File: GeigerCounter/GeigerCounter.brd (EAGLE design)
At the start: 100 x 80 mm, 5 parts, among them IC1 OPAMP-DUALU

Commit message: preliminary schematic work
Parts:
- added C2, C3, C4, C5, C6: (no value), SparkFun-Passives:CAP-PTH-SMALL2
- added H1, H2, H3, H4: MOUNT-HOLE3.0, holes:3,0
- added IC2: OPAMP-DUALU, SparkFun-AnalogIC:SO08
- added R10, R11, R12, R13, R14, R15, R16, R18, R19, R2, R20, R22, R3, R4, R5, R6, R7, R8, R9: (no value), SparkFun-Passives:AXIAL-0.3
- moved C1 68.7 mm to (-53.5, -47.4)
- moved R1 64.9 mm to (-44.7, -43.7)
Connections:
- removed net V+: IC1.8
- removed net V-: IC1.4
- new net N$1: C3.2, R3.P$1
- new net N$10: C4.2, IC2.1, R12.P$2, R14.P$2, R15.P$1
- new net N$11: C4.1, IC2.2, R12.P$1, R14.P$1
- new net N$12: C5.1, R15.P$2
- new net N$13: C5.2, R13.P$1
- new net N$14: C6.1, IC2.6, R18.P$1, R19.P$1, R8.P$2
- new net N$15: C6.2, IC2.7, R18.P$2, R19.P$2, R20.P$1
- new net N$2: D1.A, R9.P$1
- new net N$3: C2.2, IC1.1, R10.P$2, R11.P$1, R2.P$2
- new net N$4: IC2.5, R13.P$2, R16.P$2
- new net N$5: D1.C, R22.P$1
- new net N$6: C2.1, IC1.2, R10.P$1, R2.P$1
- new net N$7: C3.1, R11.P$2
- new net N$8: C1.1, IC1.6, R3.P$2, R5.P$1, R6.P$1
- new net N$9: C1.2, IC1.7, R5.P$2, R6.P$2, R7.P$1
- new net VCC_1.25: IC1.3, IC1.5, R1.P$2, R4.P$1
- net GND: now also IC1.4, IC2.3, IC2.4, R1.P$1, R16.P$1, R8.P$1
- net VCC: now also IC1.8, IC2.8, R4.P$2

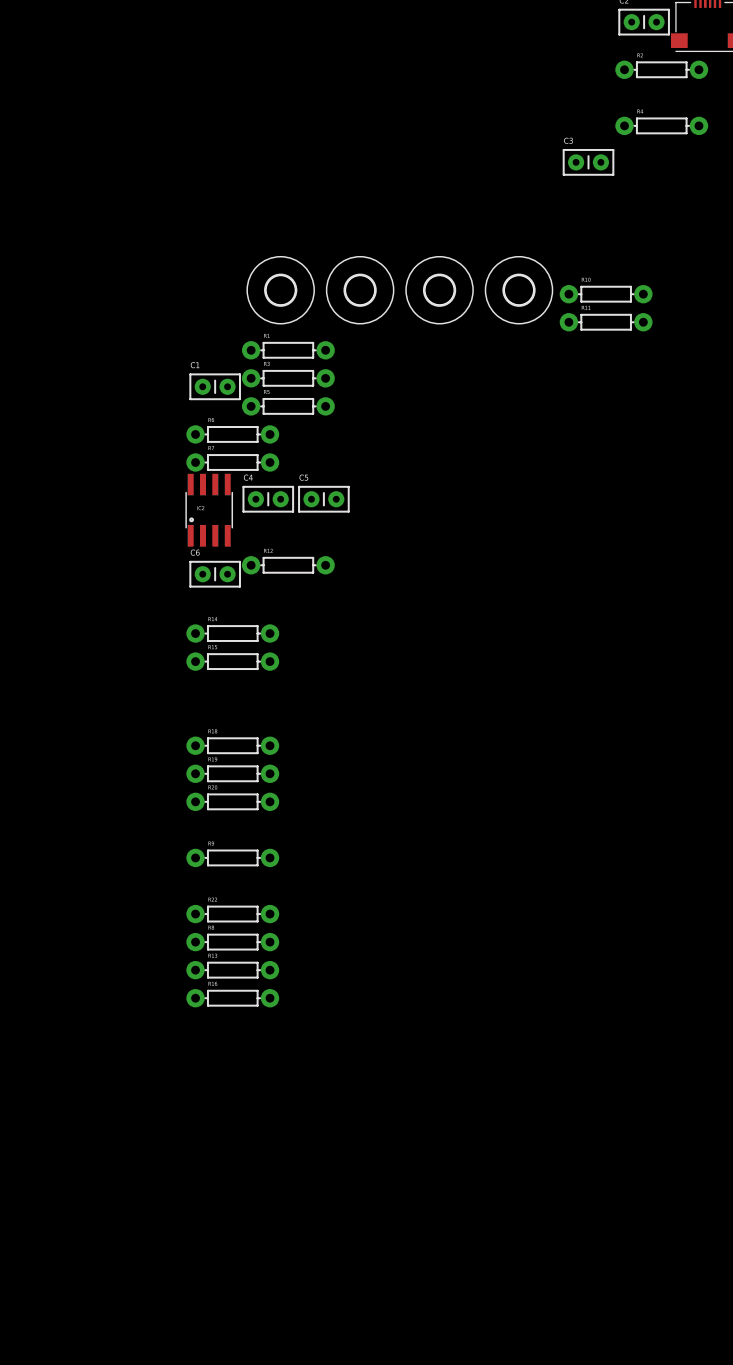
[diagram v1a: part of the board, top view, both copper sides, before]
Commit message: all components placed in schematic
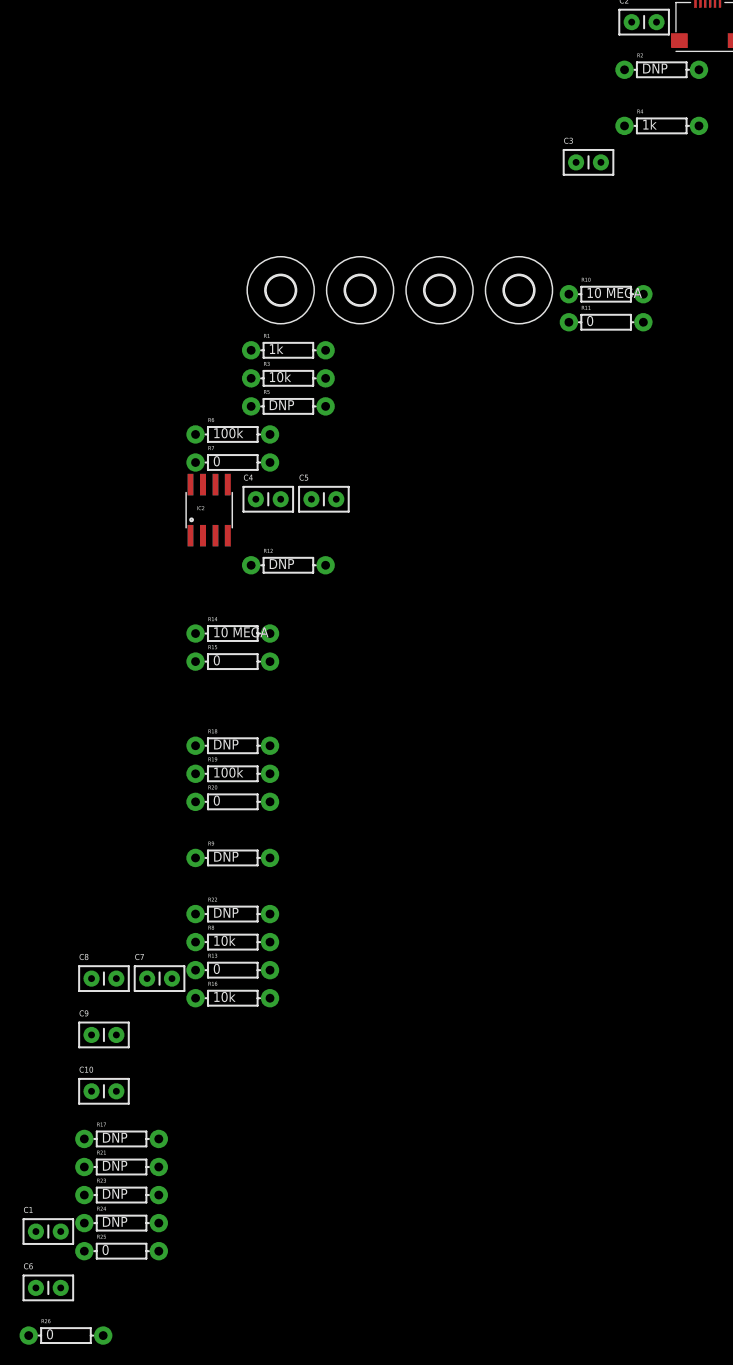
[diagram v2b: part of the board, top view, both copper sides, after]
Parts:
- added C10, C8: 0.1uF, SparkFun-Passives:CAP-PTH-SMALL2
- added C7, C9: 2.2uF, SparkFun-Passives:CAP-PTH-SMALL2
- added R17, R21, R23, R24: DNP, SparkFun-Passives:AXIAL-0.3
- added R25, R26: 0, SparkFun-Passives:AXIAL-0.3
- C1, C6, R12, R18, R2, R22, R5, R9: value (none) -> DNP
- C2, C4: value (none) -> 2pF
- C3, C5: value (none) -> 100pF
- R1, R4: value (none) -> 1k
- R10, R14: value (none) -> 10 MEGA
- R11, R13, R15, R20, R7: value (none) -> 0
- R16, R3, R8: value (none) -> 10k
- R19, R6: value (none) -> 100k
- moved C1 88.1 mm to (-70.6, -133.9)
- moved C6 75.0 mm to (-70.6, -139.6)
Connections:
- new net N$16: R26.P$1, R7.P$2
- new net N$17: C1.1, R24.P$1, R25.P$2
- new net N$20: C6.1, R23.P$1, R26.P$2
- new net N$21: R20.P$2, R25.P$1
- net GND: now also C1.2, C10.1, C6.2, C7.1, C8.1, C9.1, R9.P$2
- net N$11: now also R21.P$2
- net N$14: no longer C6.1
- net N$15: no longer C6.2
- net N$2: now also R17.P$1
- net N$5: now also R21.P$1
- net N$6: now also R17.P$2
- net N$8: no longer C1.1
- net N$9: no longer C1.2
- net P3.4: now also R24.P$2
- net P3.5: now also R23.P$2
- net VCC: now also C10.2, C7.2, C8.2, C9.2
- net VCC_1.25: now also R22.P$2

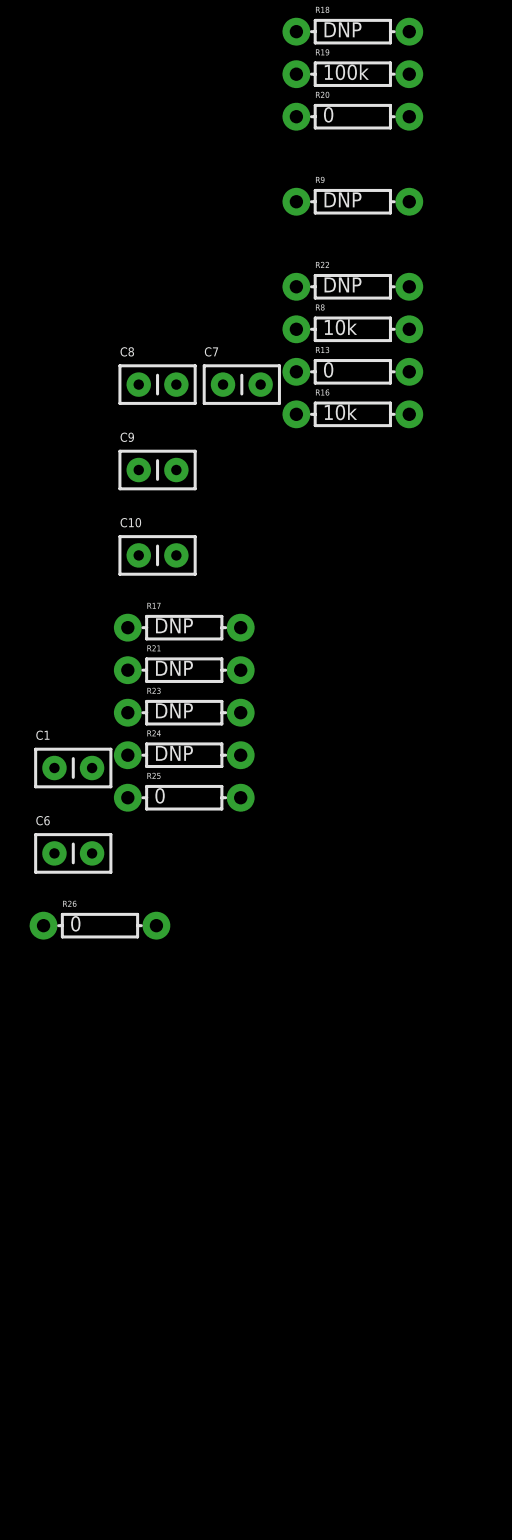
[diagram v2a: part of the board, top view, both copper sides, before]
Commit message: Added header pins as well as cleaned up schematic a bit. Also added test points
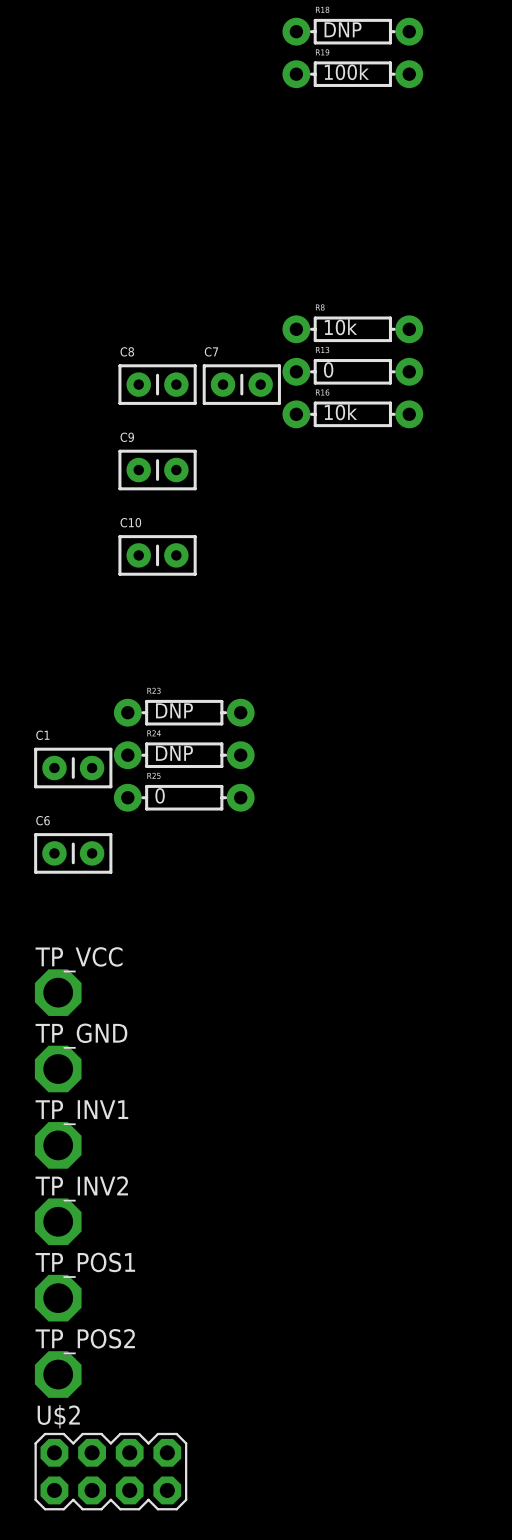
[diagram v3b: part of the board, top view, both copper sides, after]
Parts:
- removed R17, R21, R22, R9: DNP, SparkFun-Passives:AXIAL-0.3
- removed R20, R26: 0, SparkFun-Passives:AXIAL-0.3
- added TP_GND, TP_INV1, TP_INV2, TP_POS1, TP_POS2, TP_VCC: PTR1PAD1-20, testpad:P1-20
- added U$2: M04X2, SparkFun-Connectors:2X4
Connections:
- removed net N$20: C6.1, R23.P$1, R26.P$2
- removed net N$21: R20.P$2, R25.P$1
- net GND: now also TP_GND.TP, U$2.4; no longer R9.P$2
- net N$11: now also U$2.8; no longer R21.P$2
- net N$12: now also TP_POS1.TP
- net N$15: now also R25.P$1, TP_POS2.TP; no longer R20.P$1
- net N$16: now also C6.1, R23.P$1; no longer R26.P$1
- net N$2: now also D1.C, U$2.5, U$2.7; no longer D1.A, R17.P$1, R9.P$1
- net N$5: now also D1.A, U$2.1, U$2.3; no longer D1.C, R21.P$1, R22.P$1
- net N$6: now also U$2.2; no longer R17.P$2
- net N$7: now also TP_INV1.TP
- net N$9: now also TP_INV2.TP
- net VCC: now also TP_VCC.TP
- net VCC_1.25: now also U$2.6; no longer R22.P$2

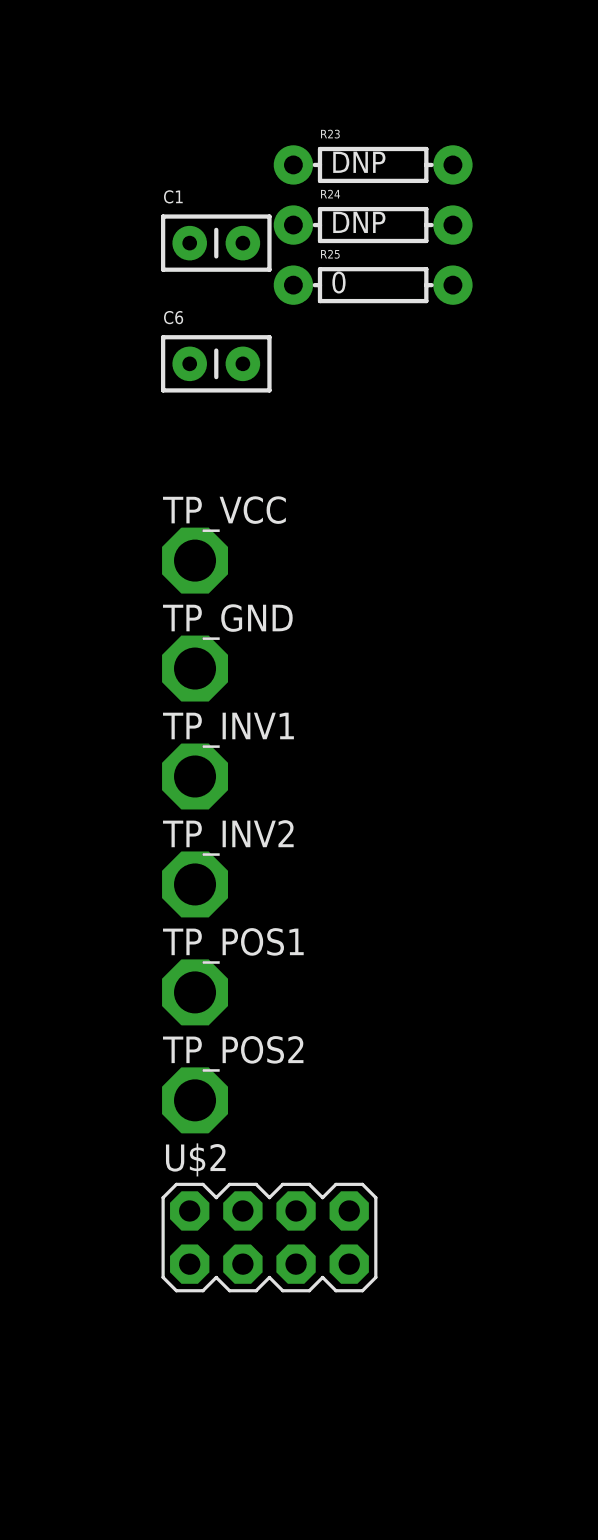
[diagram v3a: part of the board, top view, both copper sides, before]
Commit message: Updated with new connector on output
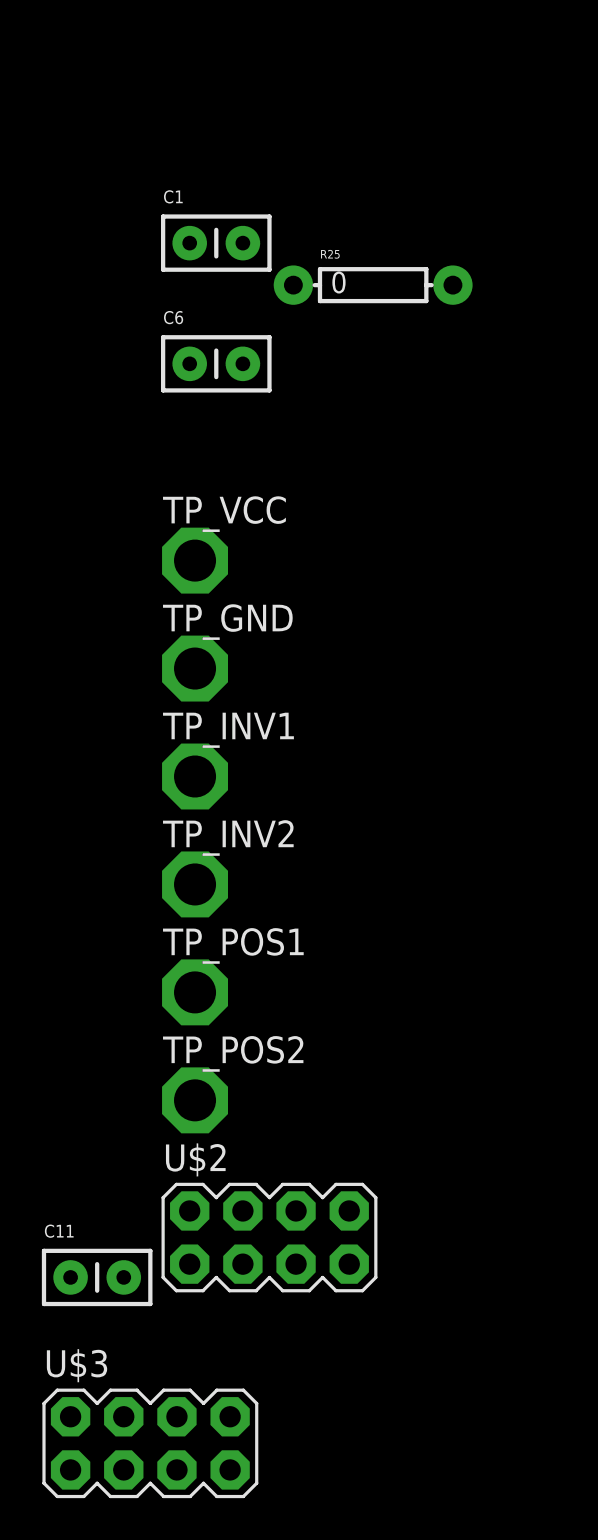
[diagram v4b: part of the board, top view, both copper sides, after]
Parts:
- removed R23, R24: DNP, SparkFun-Passives:AXIAL-0.3
- added C11: 0.1uF, SparkFun-Passives:CAP-PTH-SMALL2
- added U$3: M04X2, SparkFun-Connectors:2X4
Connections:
- new net NC1: U$1.2, U$3.2
- new net NC2: U$1.4, U$3.6
- net GND: now also C11.1
- net N$16: now also U$3.1, U$3.3; no longer R23.P$1
- net N$17: now also U$3.5, U$3.7; no longer R24.P$1
- net P3.4: now also U$3.8; no longer R24.P$2
- net P3.5: now also U$3.4; no longer R23.P$2
- net VCC_1.25: now also C11.2
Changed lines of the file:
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@@
 <element name="C9" library="SparkFun-Passives" package="CAP-PTH-SMALL2" value="2.2uF" x="-64.8716" y="-113.7412"/>
 <element name="C10" library="SparkFun-Passives" package="CAP-PTH-SMALL2" value="0.1uF" x="-64.8716" y="-119.507"/>
-<element name="R23" library="SparkFun-Passives" package="AXIAL-0.3" value="DNP" x="-61.7982" y="-130.1242"/>
-<element name="R24" library="SparkFun-Passives" package="AXIAL-0.3" value="DNP" x="-61.7982" y="-132.9944"/>
 <element name="R25" library="SparkFun-Passives" package="AXIAL-0.3" value="0" x="-61.7982" y="-135.8646"/>
 <element name="C1" library="SparkFun-Passives" package="CAP-PTH-SMALL2" value="DNP" x="-70.5612" y="-133.858"/>
@@
 </element>
 <element name="U$2" library="SparkFun-Connectors" package="2X4" value="M04X2" x="-66.7512" y="-181.356"/>
+<element name="C11" library="SparkFun-Passives" package="CAP-PTH-SMALL2" value="0.1uF" x="-76.2508" y="-183.261"/>
+<element name="U$3" library="SparkFun-Connectors" package="2X4" value="M04X2" x="-72.4408" y="-191.1858"/>
 </elements>
 <signals>
@@
 <contactref element="TP_GND" pad="TP"/>
 <contactref element="U$2" pad="4"/>
+<contactref element="C11" pad="1"/>
+<wire x1="-76.2508" y1="-183.261" x2="-68.0212" y2="-180.086" width="0" layer="19" extent="1-1"/>
 <wire x1="-70.3072" y1="-154.178" x2="-68.0212" y2="-180.086" width="0" layer="19" extent="1-1"/>
 <wire x1="-68.0212" y1="-139.6238" x2="-70.3072" y2="-154.178" width="0" layer="19" extent="1-1"/>
@@
 <signal name="P3.5">
 <contactref element="U$1" pad="3"/>
-<contactref element="R23" pad="P$2"/>
-<wire x1="-2.0734" y1="-8.1026" x2="-57.9882" y2="-130.1242" width="0" layer="19" extent="1-1"/>
+<contactref element="U$3" pad="4"/>
+<wire x1="-73.7108" y1="-189.9158" x2="-2.0734" y2="-8.1026" width="0" layer="19" extent="1-1"/>
 </signal>
 <signal name="P3.4">
 <contactref element="U$1" pad="5"/>
-<contactref element="R24" pad="P$2"/>
-<wire x1="-1.0734" y1="-8.1026" x2="-57.9882" y2="-132.9944" width="0" layer="19" extent="1-1"/>
+<contactref element="U$3" pad="8"/>
+<wire x1="-68.6308" y1="-189.9158" x2="-1.0734" y2="-8.1026" width="0" layer="19" extent="1-1"/>
 </signal>
 <signal name="N$3">
@@
 <contactref element="IC1" pad="3"/>
 <contactref element="U$2" pad="6"/>
+<contactref element="C11" pad="2"/>
+<wire x1="-73.7108" y1="-183.261" x2="-65.4812" y2="-180.086" width="0" layer="19" extent="1-1"/>
 <wire x1="-40.9194" y1="-43.688" x2="-65.4812" y2="-180.086" width="0" layer="19" extent="1-1"/>
 <wire x1="-10.3378" y1="-20.7264" x2="-40.9194" y2="-43.688" width="0" layer="19" extent="1-1"/>
@@
 <contactref element="R25" pad="P$2"/>
 <contactref element="C1" pad="1"/>
-<contactref element="R24" pad="P$1"/>
-<wire x1="-65.6082" y1="-132.9944" x2="-70.5612" y2="-133.858" width="0" layer="19" extent="1-1"/>
-<wire x1="-57.9882" y1="-135.8646" x2="-65.6082" y2="-132.9944" width="0" layer="19" extent="1-1"/>
+<contactref element="U$3" pad="7"/>
+<contactref element="U$3" pad="5"/>
+<wire x1="-57.9882" y1="-135.8646" x2="-70.5612" y2="-133.858" width="0" layer="19" extent="1-1"/>
+<wire x1="-68.6308" y1="-192.4558" x2="-57.9882" y2="-135.8646" width="0" layer="19" extent="1-1"/>
+<wire x1="-71.1708" y1="-192.4558" x2="-68.6308" y2="-192.4558" width="0" layer="19" extent="1-1"/>
 </signal>
 <signal name="N$16">
 <contactref element="R7" pad="P$2"/>
 <contactref element="C6" pad="1"/>
-<contactref element="R23" pad="P$1"/>
-<wire x1="-65.6082" y1="-130.1242" x2="-70.5612" y2="-139.6238" width="0" layer="19" extent="1-1"/>
-<wire x1="-46.609" y1="-55.1688" x2="-65.6082" y2="-130.1242" width="0" layer="19" extent="1-1"/>
+<contactref element="U$3" pad="1"/>
+<contactref element="U$3" pad="3"/>
+<wire x1="-73.7108" y1="-192.4558" x2="-70.5612" y2="-139.6238" width="0" layer="19" extent="1-1"/>
+<wire x1="-76.2508" y1="-192.4558" x2="-73.7108" y2="-192.4558" width="0" layer="19" extent="1-1"/>
+<wire x1="-46.609" y1="-55.1688" x2="-70.5612" y2="-139.6238" width="0" layer="19" extent="1-1"/>
 </signal>
 <signal name="N$2">
@@
 <wire x1="-4.5974" y1="-5.334" x2="-68.0212" y2="-182.626" width="0" layer="19" extent="1-1"/>
 </signal>
+<signal name="NC1">
+<contactref element="U$1" pad="2"/>
+<contactref element="U$3" pad="2"/>
+<wire x1="-76.2508" y1="-189.9158" x2="-2.5734" y2="-8.1026" width="0" layer="19" extent="1-1"/>
+</signal>
+<signal name="NC2">
+<contactref element="U$1" pad="4"/>
+<contactref element="U$3" pad="6"/>
+<wire x1="-71.1708" y1="-189.9158" x2="-1.5734" y2="-8.1026" width="0" layer="19" extent="1-1"/>
+</signal>
 </signals>
